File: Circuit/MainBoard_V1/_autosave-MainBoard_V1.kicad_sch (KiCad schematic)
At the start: 118 parts, among them J1 Conn_01x07, J10 Conn_01x04, J11 Conn_01x04, J12 Conn_01x04, J13 Conn_01x04, J14 Conn_01x04, J15 Conn_01x02, J2 Conn_01x04, J3 Conn_01x04, J4 Conn_01x04, J5 Conn_01x04, J6 Raspberry_Pi_2_3, J7 Conn_01x04, J8 Conn_01x04, J9 Conn_01x04, Q1 Q_PMOS_GDS, Q2 Q_PMOS_GDS, Q3 BSS138, Q4 BSS138, Q5 BSS138, Q6 BSS138, Q7 BSS138, SW1 SW_Push, SW2 SW_Push, SW3 SW_Push, SW4 SW_Slide_DPDT, SW5 SW_Slide_DPDT, SW6 SW_Push, U1 STM32F446RETx, U2 LM1117MP-3.3, U3 MPU-6050, Y1 CSTNE16M0V530000R0

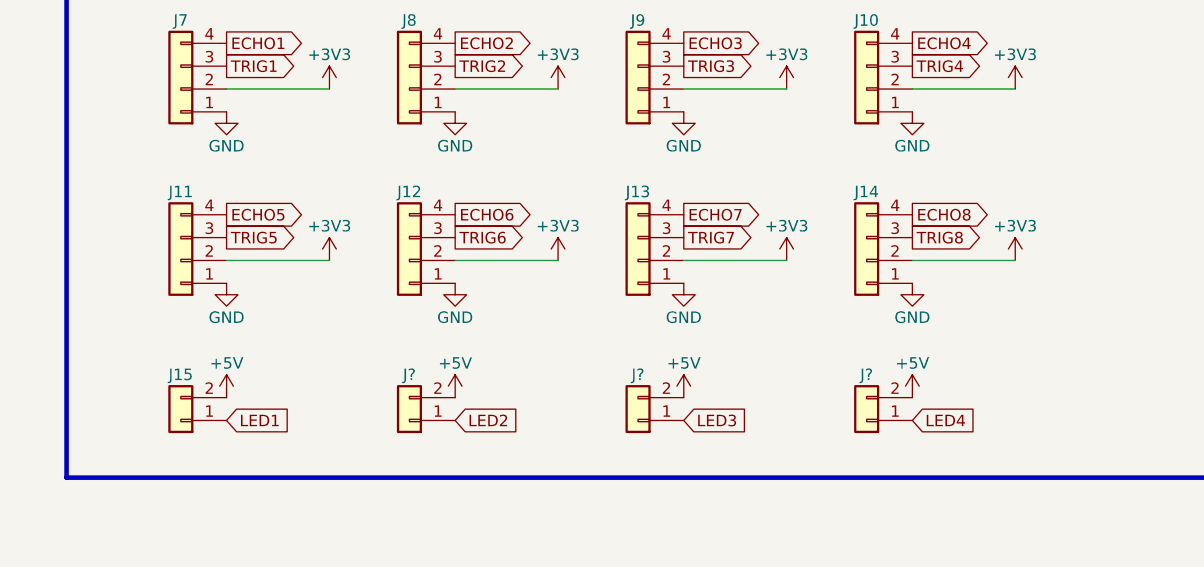
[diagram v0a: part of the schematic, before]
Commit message: LED用のコネクタ追加
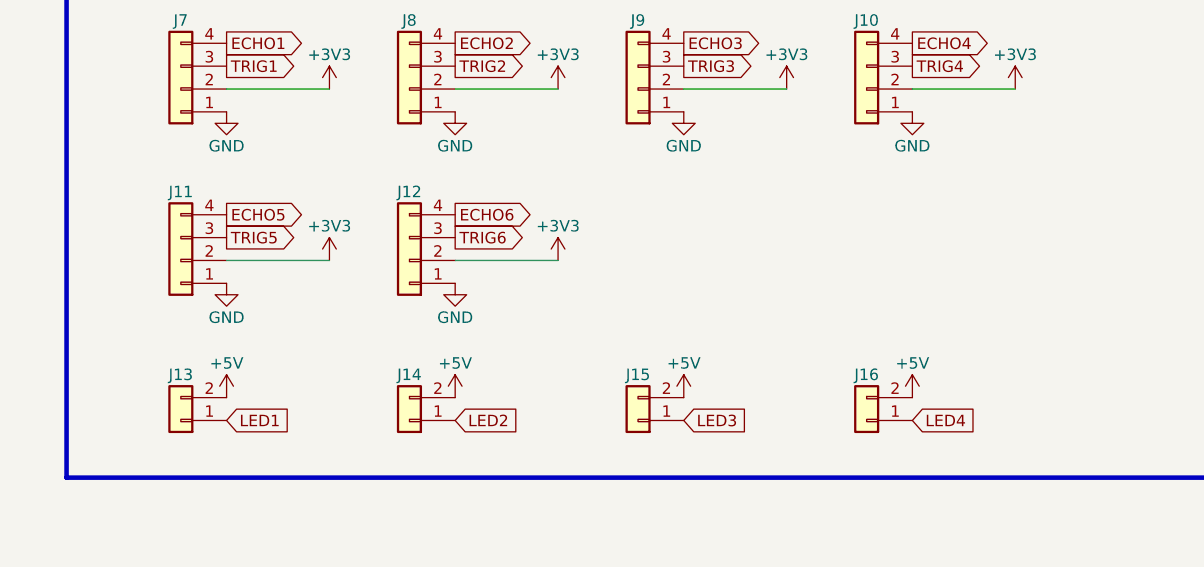
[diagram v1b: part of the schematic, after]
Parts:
- removed J13, J14: Conn_01x04, Connector_JST:JST_XH_B4B-XH-A_1x04_P2.50mm_Vertical, symbol Connector_Generic:Conn_01x04
- gave numbers to parts that had none: 3
- renumbered J15 to J13
